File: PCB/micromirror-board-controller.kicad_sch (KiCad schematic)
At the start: 18 parts, among them J1 RPi header, J2 Conn_01x04_Female, J3 Conn_01x03_Female, J4 51-pin conn, J5 Barrel_Jack, J7 5V Ext, J8 Conn_01x04_Socket

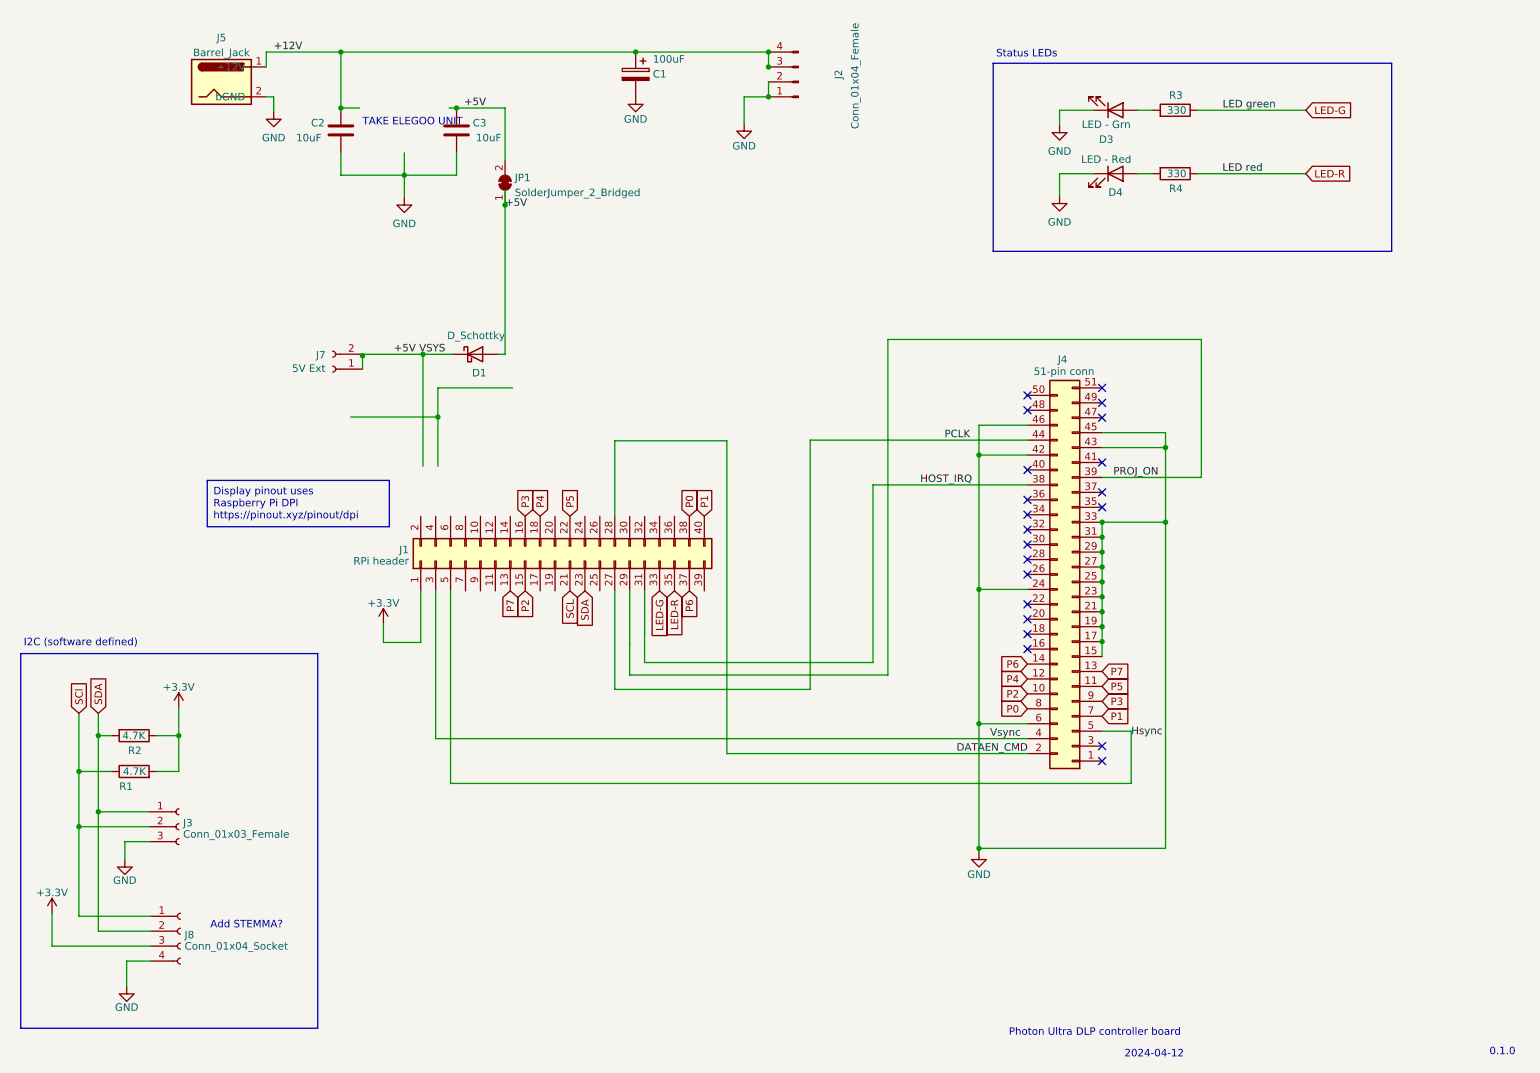
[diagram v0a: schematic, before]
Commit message: functional parallel routing
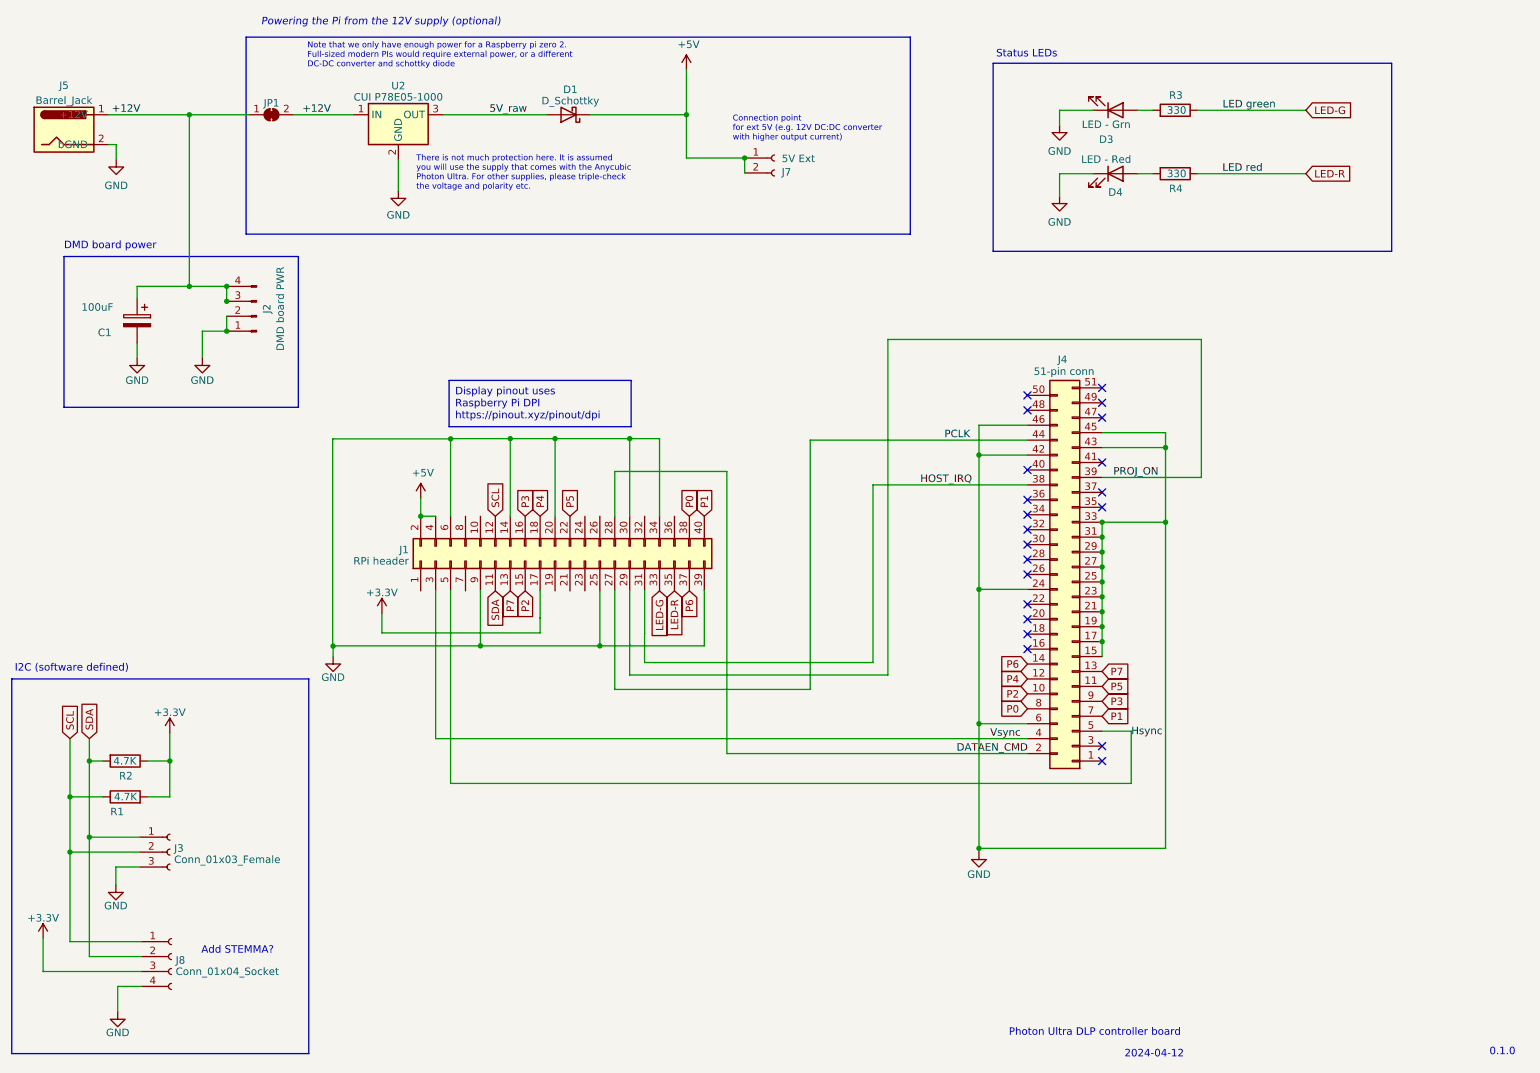
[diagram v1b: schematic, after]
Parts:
- removed C2, C3: 10uF, Capacitor_SMD:C_0805_2012Metric_Pad1.18x1.45mm_HandSolder, symbol Device:C
- added U2: CUI P78E05-1000, Converter_DCDC:Converter_DCDC_RECOM_R-78E-0.5_THT, symbol Converter_DCDC:OKI-78SR-3.3_1.5-W36-C
- D1: Mouser https://nl.mouser.com/ProductDetail/Nexperia/BAT760115?qs=m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 -> 771-PMEG1020EJ-T/R
- J2: value Conn_01x04_Female -> DMD board PWR
- JP1: footprint Jumper:SolderJumper-2_P1.3mm_Bridged_RoundedPad1.0x1.5mm -> Jumper:SolderJumper-2_P1.3mm_Open_TrianglePad1.0x1.5mm
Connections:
- net +5V VSYS is gone; now on net +5V: D1.1 (K), J7.1 (Pin_1), J7.2 (Pin_2)
- net SCl is gone; now on net SCL: J3.2 (SCL), J8.1 (Pin_1), R1.1
- net +12V: now also JP1.1 (A), JP1.2 (B), U2.1 (IN)
- net +3.3V: now also J1.17 (Pin_17); no longer J1.1 (Pin_1)
- net +5V: now also J1.2 (Pin_2), J1.4 (Pin_4); no longer D1.2 (A), JP1.1 (A), JP1.2 (B)
- net GND: now also J1.14 (Pin_14), J1.20 (Pin_20), J1.25 (Pin_25), J1.30 (Pin_30), J1.34 (Pin_34), J1.39 (Pin_39), J1.6 (Pin_6), J1.9 (Pin_9), U2.2 (GND)
- net SCL: now also J1.12 (Pin_12); no longer J1.21 (Pin_21)
- net SDA: now also J1.11 (Pin_11); no longer J1.23 (Pin_23)
- new net 5V_raw: D1.2 (A), U2.3 (OUT)
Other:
- note added: "Connection point for ext 5V (e.g. 12V DC:DC converter with higher output current)"
- note added: "DMD board power"
- note added: "Note that we only have enough power for a Raspberry pi zero 2. Full-sized modern PIs would require external power, or a different DC-DC converter and schottky diode"
- note added: "Powering the Pi from the 12V supply (optional)"
- note added: "There is not much protection here. It is assumed you will use the supply that comes with the Anycubic Photon Ultra. For other supplies, please triple-check the voltage and polarity etc."
- note removed: "TAKE ELEGOO UNIT"
- moved on the sheet: C1, J2, J3, J5, J7, J8, R1, R2

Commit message: Completed routing and schematic
Did all the routing for the board. Schematic also close to final.
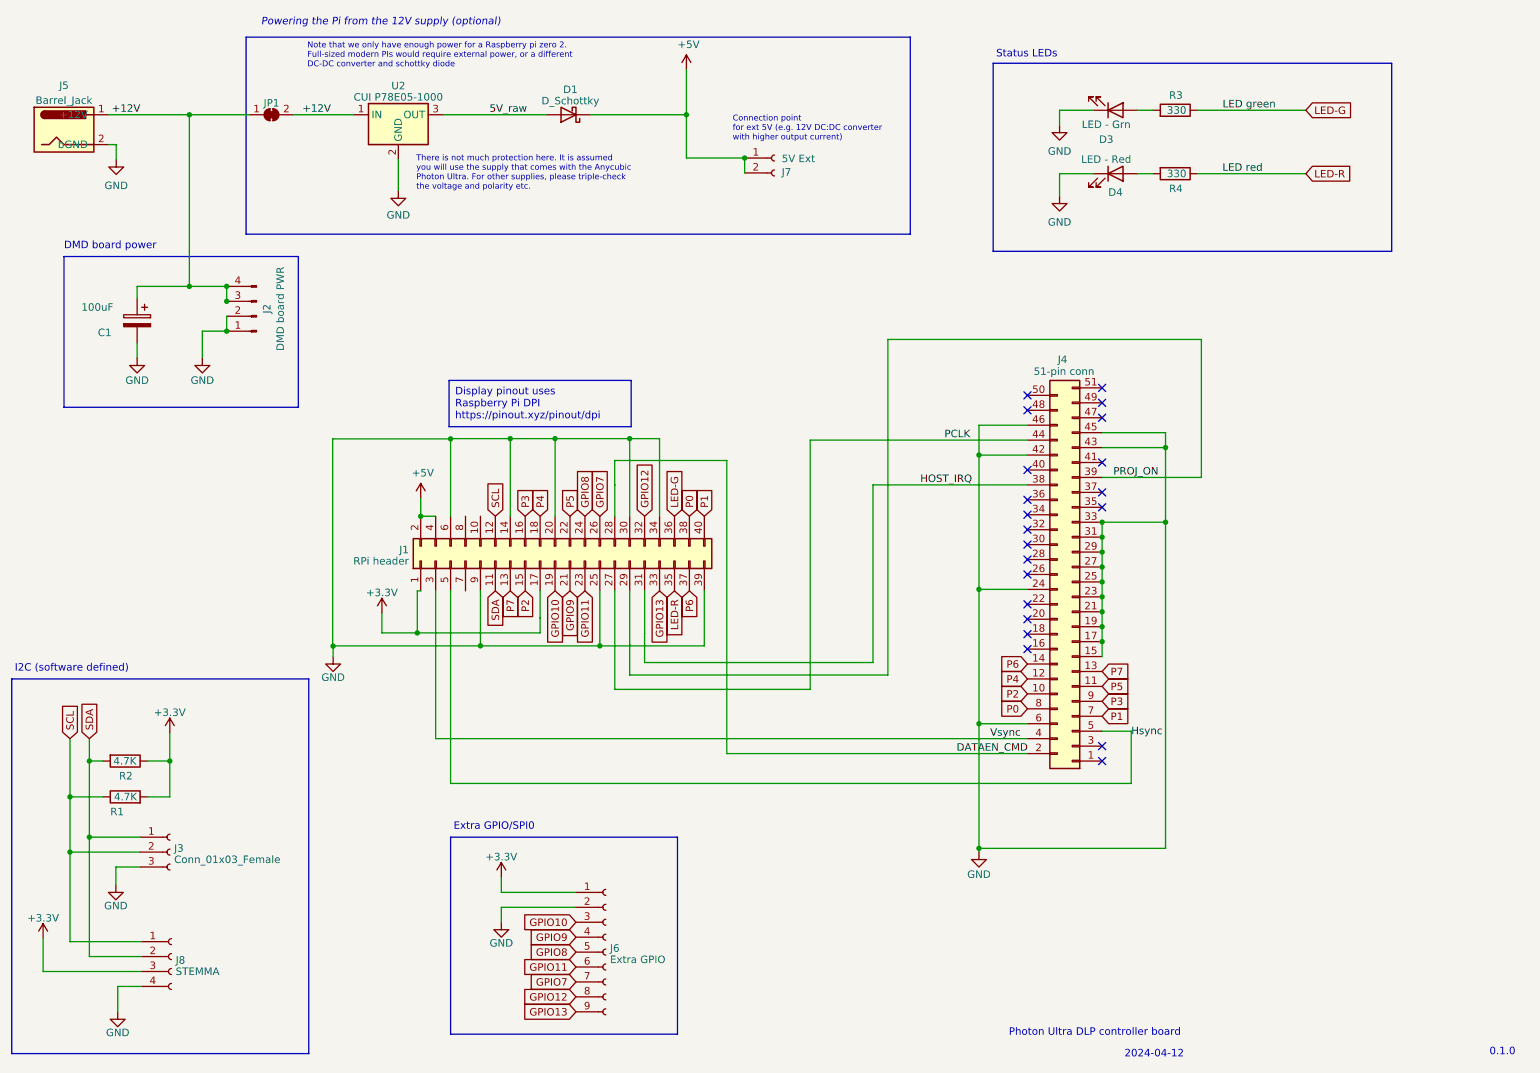
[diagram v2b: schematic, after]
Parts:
- added J6: Extra GPIO, Connector_PinHeader_2.54mm:PinHeader_1x09_P2.54mm_Vertical, symbol Connector:Conn_01x09_Socket
- J8: value Conn_01x04_Socket -> STEMMA; footprint Connector_JST:JST_SH_SM04B-SRSS-TB_1x04-1MP_P1.00mm_Horizontal -> Connector_JST:JST_SH_BM04B-SRSS-TB_1x04-1MP_P1.00mm_Vertical
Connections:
- net +3.3V: now also J1.1 (Pin_1), J6.1 (Pin_1)
- net GND: now also J6.2 (Pin_2)
- net LED-G: now also J1.36 (Pin_36); no longer J1.33 (Pin_33)
- net GPIO10: now reaches J1.19 (Pin_19)
- net GPIO10: now also J6.3 (Pin_3)
- net GPIO9: now reaches J1.21 (Pin_21)
- net GPIO9: now also J6.4 (Pin_4)
- net GPIO11: now reaches J1.23 (Pin_23)
- net GPIO11: now also J6.6 (Pin_6)
- net GPIO8: now reaches J1.24 (Pin_24)
- net GPIO8: now also J6.5 (Pin_5)
- net GPIO7: now reaches J1.26 (Pin_26)
- net GPIO7: now also J6.7 (Pin_7)
- net GPIO12: now reaches J1.32 (Pin_32)
- net GPIO12: now also J6.8 (Pin_8)
- new net GPIO13: J1.33 (Pin_33), J6.9 (Pin_9)
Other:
- note added: "Extra GPIO/SPI0"
- note removed: "Add STEMMA?"

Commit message: Add BOM
Add the bill of materials. Fixed some of the part number formatting in the schematic.
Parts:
- D3: Mouser https://nl.mouser.com/ProductDetail/Wurth-Elektronik/150080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 -> 710-150080VS75000
- D4: Mouser https://nl.mouser.com/ProductDetail/Wurth-Elektronik/150080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 -> 710-150080RS75000
- J2: Mouser https://nl.mouser.com/ProductDetail/Adafruit/4390?qs=xZ%2FP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 -> 485-4390; Mouser-link (none) -> https://nl.mouser.com/ProductDetail/Adafruit/4390?qs=xZ%2FP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
- J3: Mouser https://nl.mouser.com/ProductDetail/Adafruit/4389?qs=xZ%2FP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 -> 485-4389; Mouser-link (none) -> https://nl.mouser.com/ProductDetail/Adafruit/4389?qs=xZ%2FP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
- J8: Mouser (none) -> 474-PRT-16766
- R2: Mouser https://nl.mouser.com/ProductDetail/Panasonic/ERA-8AEB472V?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 -> 667-ERA-8AEB472V; Mouser-link (none) -> https://nl.mouser.com/ProductDetail/Panasonic/ERA-8AEB472V?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
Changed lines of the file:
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@@
+      (effects (font (size 1.27 1.27)) hide)
+    )
+    (property "Mouser" "474-PRT-16766" (at 44.196 176.784 0)
+      (effects (font (size 1.27 1.27)) hide)
+    )
+    (property "Field5" "" (at 44.196 176.784 0)
       (effects (font (size 1.27 1.27)) hide)
     )
@@
       (effects (font (size 1.27 1.27)) hide)
     )
-    (property "Mouser" "https://nl.mouser.com/ProductDetail/Wurth-Elektronik/150080RS75000?qs=LlUlMxKIyB2jdCo7bnfgew%3D%3D" (at 204.851 43.561 0)
+    (property "Mouser" "710-150080RS75000" (at 204.851 43.561 0)
       (effects (font (size 1.27 1.27)) hide)
     )
@@
       (effects (font (size 1.27 1.27)) hide)
     )
-    (property "Mouser" "https://nl.mouser.com/ProductDetail/Wurth-Elektronik/150080VS75000?qs=LlUlMxKIyB0tGHJmO6%252B0ug%3D%3D" (at 204.851 32.766 0)
+    (property "Mouser" "710-150080VS75000" (at 204.851 32.766 0)
       (effects (font (size 1.27 1.27)) hide)
     )
@@
       (effects (font (size 1.27 1.27)) hide)
     )
-    (property "Mouser" "https://nl.mouser.com/ProductDetail/Panasonic/ERA-8AEB472V?qs=Ojoo2rCVP9Sy1lUSq6%252B0Xg%3D%3D" (at 36.322 143.51 0)
+    (property "Mouser-link" "https://nl.mouser.com/ProductDetail/Panasonic/ERA-8AEB472V?qs=Ojoo2rCVP9Sy1lUSq6%252B0Xg%3D%3D" (at 36.322 143.51 0)
+      (effects (font (size 1.27 1.27)) hide)
+    )
+    (property "Mouser" "667-ERA-8AEB472V" (at 36.322 143.51 90)
+      (effects (font (size 1.27 1.27)) hide)
+    )
+    (property "Field6" "" (at 36.322 143.51 90)
       (effects (font (size 1.27 1.27)) hide)
     )
@@
       (effects (font (size 1.27 1.27)) hide)
     )
-    (property "Mouser" "https://nl.mouser.com/ProductDetail/Adafruit/4389?qs=xZ%2FP%252Ba9zWqbz84%252BdNJD1Eg%3D%3D" (at 43.942 159.004 0)
+    (property "Mouser-link" "https://nl.mouser.com/ProductDetail/Adafruit/4389?qs=xZ%2FP%252Ba9zWqbz84%252BdNJD1Eg%3D%3D" (at 43.942 159.004 0)
+      (effects (font (size 1.27 1.27)) hide)
+    )
+    (property "Mouser" "485-4389" (at 43.942 159.004 0)
+      (effects (font (size 1.27 1.27)) hide)
+    )
+    (property "Field6" "" (at 43.942 159.004 0)
       (effects (font (size 1.27 1.27)) hide)
     )
@@
       (effects (font (size 1.27 1.27)) hide)
     )
-    (property "Mouser" "https://nl.mouser.com/ProductDetail/Adafruit/4390?qs=xZ%2FP%252Ba9zWqaq7Vo4%2FzdP%252BA%3D%3D" (at 58.674 67.818 0)
-      (effects (font (size 1.27 1.27)) hide)
-    )
+    (property "Mouser-link" "https://nl.mouser.com/ProductDetail/Adafruit/4390?qs=xZ%2FP%252Ba9zWqaq7Vo4%2FzdP%252BA%3D%3D" (at 58.674 67.818 0)
+      (effects (font (size 1.27 1.27)) hide)
+    )
+    (property "Mouser" "485-4390" (at 58.674 67.818 90)
+      (effects (font (size 1.27 1.27)) hide)
+    )
+    (property "Field6" "" (at 58.674 67.818 90)
+      (effects (font (size 1.27 1.27)) hide)
+    )
